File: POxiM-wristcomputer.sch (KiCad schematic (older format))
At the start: 25 parts, among them J1 USB_B_Micro, J10 Transmissivity in, J11 AudioJack4_Ground, J2 AudioJack4_Ground, J3 USB_B_Micro, J4 USB_A, J5 USB_A, J6 Uart Out, J7 Programming Header, J8 USB_B_Micro, J9 Interference in

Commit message: Start new LED drive method, some cleanup
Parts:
- removed J10: Transmissivity in, Connector_Coaxial:SMA_Molex_73251-2200_Horizontal, symbol Connector:Conn_Coaxial
- removed J11, J2: AudioJack4_Ground, POxiM-uncategorised:CUI_SJ-43514-SMT, symbol Connector:AudioJack4_Ground
- removed J3, J8: USB_B_Micro, POxiM-uncategorised:Micro-B_Molex_105017-0001, symbol Connector:USB_B_Micro
- removed J4, J5: USB_A, POxiM-uncategorised:USBA_87583-2010RLF, symbol Connector:USB_A
- removed J6: Uart Out, Connector_PinHeader_2.54mm:PinHeader_1x02_P2.54mm_Vertical, symbol Connector:Conn_01x02_Male
- removed J7: Programming Header, Connector_PinHeader_2.54mm:PinHeader_2x05_P2.54mm_Vertical, symbol Connector:Conn_01x10_Male
- removed J9: Interference in, Connector_Coaxial:SMA_Molex_73251-2200_Horizontal, symbol Connector:Conn_Coaxial
- removed MB1, MB2, MB3, MB4, MB5, MB6, MB7, MB8: Bumpon, POxiM-uncategorised:Bumpon-SJ-5007BK, symbol POxiM-mechanical:Bumpon
- added J?: To finger probe, POxiM-uncategorised:CUI_SJ-43514-SMT, symbol Connector:AudioJack4
- J1: value USB_B_Micro -> Power in
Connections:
- net labels removed: 5V_power_input
- wire segments 92 -> 32
- no-connect marks 11 -> 1
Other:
- note added: "Audio\npinout:"
- note added: "Ground"
- note added: "Left"
- note added: "Mechanical"
- note added: "Mic"
- note added: "Right"
- note removed: "Finger pretender board"
- note removed: "Programming board"
- note removed: "for audio:\nmic\ngnd\nright\nleft\n"
- moved on the sheet: H1, H2, H3, H4, H5, H6, J1

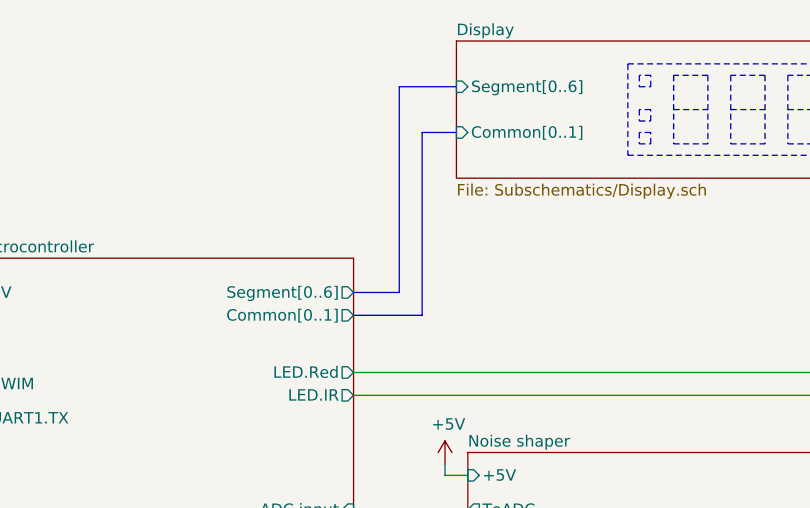
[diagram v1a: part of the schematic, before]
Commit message: Finish signal conditioning cleanup, start reworking display
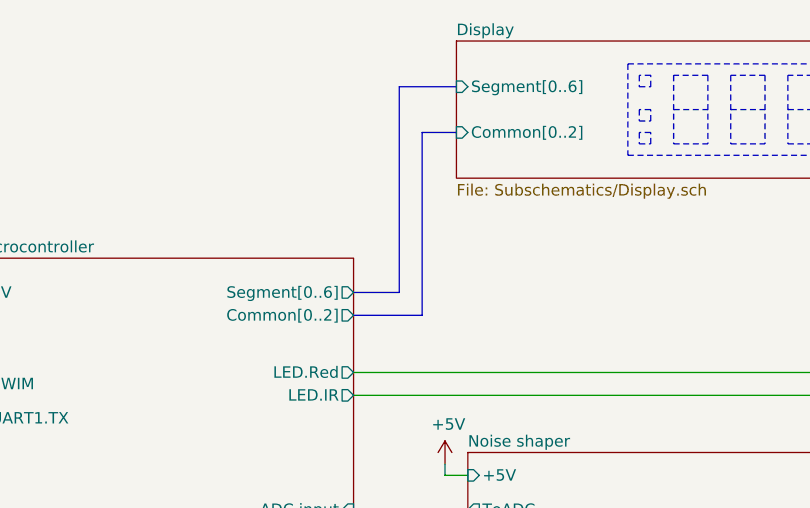
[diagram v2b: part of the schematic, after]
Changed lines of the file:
@@
 F1 "Subschematics/Display.sch" 50
 F2 "Segment[0..6]" I L 5750 2400 50
-F3 "Common[0..1]" I L 5750 2600 50
+F3 "Common[0..2]" I L 5750 2600 50
 $EndSheet
 $Sheet
@@
 F3 "5V" I L 3650 3300 50
 F4 "Segment[0..6]" O R 5300 3300 50
-F5 "Common[0..1]" O R 5300 3400 50
-F6 "ADC.feedback" O R 5300 4350 50
-F7 "ADC.input" I R 5300 4250 50
-F8 "LED.IR" O R 5300 3750 50
-F9 "LED.Red" O R 5300 3650 50
-F10 "UART1.TX" O L 3650 3850 50
-F11 "SWIM" B L 3650 3700 50
+F5 "ADC.feedback" O R 5300 4350 50
+F6 "ADC.input" I R 5300 4250 50
+F7 "LED.IR" O R 5300 3750 50
+F8 "LED.Red" O R 5300 3650 50
+F9 "UART1.TX" O L 3650 3850 50
+F10 "SWIM" B L 3650 3700 50
+F11 "Common[0..2]" O R 5300 3400 50
 $EndSheet
 Wire Wire Line

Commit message: Cleanup most of schematic
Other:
- note added: "Bibliography"
- note added: "How it works"
- note added: "In response to shortages during the Covid-19 pandemic, TU Delft is \ndeveloping the POxiM transmissive pulse oximeter. A pulse oximeter is a \nmedical instrument which doctors use to monitor the heart rate and blood \noxygen saturation of patients during critical stages of and revalidation from \nCovid-19. POxiM is intended to be fully qualified for use leading up to and \nafter intensive care, t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"
- note added: "Introduction"
- note added: "POxiM is based on the tranmissive pulse oximetry principle. This means that \nit determines the patient’s heart rate and blood oxygen concentration \n(SPO2) by measuring the portion of red (660nm) and infrared (940nm) light \nthat passes through their finger.\n\nThis is enabled by two effects. First, the optical properties of hemoglobin \nchange when it bonds with oxygen, so that blood with a hig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"
- note added: "Power budget"
- note added: "The physical system"
- note added: "There is 100mA available from a\nsingle power unit of USB. It is\nallocated as follows:\n - Microcontroller: 5mA\n - Readout circuit amplifier: 1mA\n - Readout LEDs: 2 · 10mA = 20mA\n - Display: 74mA\n - Digits: 7 · 10mA = 70mA\n - Transistor biasing: 4mA"
- note added: "There is only a single optical channel to avoid the cost of optical filters and \nmultiple channels. This introduces a problem, since the channel must be \nshared between the two wavelengths. Since the noise shaping circuitry is not \ncompatible with sharing the channel in time, the channel is shared in the \nfrequency domain. This is achieved by modulating each wavelength at a \nunique carrier f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"
- note added: "This design was informed by NXP’s AN4327 appnote, TI’s SLAA655, \nSLAA274, and SLAA458 appnotes, and TI’s TIDA-00311 reference design."
- note added: "ToDo:\n - Add top-level descriptions to each sheet.\n - Improve noise shaper description.\n - Update component values for Vin ∈ [4.5, 5.5]V\n - Check PWM output harmonics actually have 60dB down, and consider adding image\n - Explain microcontroller choice"
- moved on the sheet: J1, J?

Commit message: Start reworking sing supply ripple issues.
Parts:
- added FID? (x4): Fiducial, Fiducial:Fiducial_0.5mm_Mask1mm, symbol Mechanical:Fiducial
- H1, H2, H3, H4, H5, H6: Notes (none) -> SHOULD NOT BE ON BOM
- J1: Link (none) -> https://nl.mouser.com/ProductDetail/Molex/105017-0001?qs=%2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; Mfr. Molex -> (none); Mfr. No. 105017-0001 -> (none); Mouser No. 538-105017-0001 -> (none); Order number (none) -> 538-105017-0001; Part number (none) -> 105017-0001; Supplier (none) -> Mouser
- gave numbers to parts that had none: 1
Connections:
- net +5V: no longer J2.R2
- net GND: now also J2.R2
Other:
- note added: "# ToDo\n### Schematic\n - [x] Rework display LEDs to open drain\n - [x] Add LDO\n - [x] Feed noise shaper from LDO, so it cannot damage microcontroller\n - [x] Add DAC buffer\n - [ ] Add IR/red LED supply current isolation\n - [ ] Check if Zener voltage needs to change to incorporate lower supply voltage\n - [ ] Change noise shaper + in to ground\n - [ ] Update prediction inversion\n - [ ] Change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"
- note added: "Change stereo connector?\nIk zal even rondkijken voor 3,5m stereo jack connectoren. De CUI SJ-43514 \nis een connector die ik gisteren ook tegen kwam. Dit is zeker een optie."
- note added: "De USB-connectoren die wij hier momenteel op voorraad hebben liggen:\n - ZX62D-B-5PA8 Hirose\n - 10104110-0001LF FCI (Geheel SMD, dus het liefste vastklemmen)\n - 629105136821 WUERTH (Geheel SMD, dus het liefste vastklemmen)\n - 10118194-0001L FCI"
- note added: "Microcontroller needs 3.3V LDO, since required 40dB PSRR @ 5mA cannot \nbe easily achieved with capacitance multiplier at low frequencies and small \ncapacitors, whereas a voltage reference PSRR gets better at lower \nfrequencies.\n\nLED currents should be passed through ground so that only ground bond \nwire resistance is a factor, and the 1Ω output impedance of the LDO isn’t a \nproblem.\n\nLED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"
- note added: "To muntz:\n - Test whether LED driver RC delay is really necessary."
- moved on the sheet: H1, H2, H3, H4, H5, H6

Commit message: Initial PCB layout
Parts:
- FID1, FID2, FID3, FID4: renamed from FID?; Notes (none) -> SHOULD NOT BE ON BOM
- H1, H2, H3, H4: footprint MountingHole:MountingHole_2.2mm_M2_DIN965 -> POxiM-uncategorised:MountingHole_2.2mm_M2
- H5, H6: footprint MountingHole:MountingHole_2.2mm_M2_DIN965 -> POxiM-uncategorised:AlignmentHole_2.2mm_M2
- J1: footprint POxiM-uncategorised:Micro-B_Molex_105017-0001 -> POxiM-uncategorised:USB_Micro-B_Amphenol_10103594-0001LF_Horizontal; Link https://nl.mouser.com/ProductDetail/Molex/105017-0001?qs=%2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 -> https://nl.mouser.com/ProductDetail/Amphenol-FCI/10103594-0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; Order number 538-105017-0001 -> 649-10103594-0001LF; Part number 105017-0001 -> 10103594-0001LF
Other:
- note added: "# ToDo\n### Schematic\n - [x] Rework display LEDs to open drain\n - [x] Add LDO\n - [x] Feed noise shaper from LDO, so it cannot damage microcontroller\n - [x] Add DAC buffer\n - [x] Add IR/red LED supply current isolation\n - [x] Change noise shaper + in to ground\n - [x] Update prediction inversion\n - [x] Check if Zener voltage needs to change to incorporate lower supply voltage\n - [x] Change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"
- note added: "To muntz:\n - Test whether LED driver RC delay is really necessary.\n - LED display decoupling"
- note removed: "# ToDo\n### Schematic\n - [x] Rework display LEDs to open drain\n - [x] Add LDO\n - [x] Feed noise shaper from LDO, so it cannot damage microcontroller\n - [x] Add DAC buffer\n - [ ] Add IR/red LED supply current isolation\n - [ ] Check if Zener voltage needs to change to incorporate lower supply voltage\n - [ ] Change noise shaper + in to ground\n - [ ] Update prediction inversion\n - [ ] Change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"
- note removed: "Microcontroller needs 3.3V LDO, since required 40dB PSRR @ 5mA cannot \nbe easily achieved with capacitance multiplier at low frequencies and small \ncapacitors, whereas a voltage reference PSRR gets better at lower \nfrequencies.\n\nLED currents should be passed through ground so that only ground bond \nwire resistance is a factor, and the 1Ω output impedance of the LDO isn’t a \nproblem.\n\nLED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"
- note removed: "To muntz:\n - Test whether LED driver RC delay is really necessary."
- note removed: "ToDo:\n - Add top-level descriptions to each sheet.\n - Improve noise shaper description.\n - Update component values for Vin ∈ [4.5, 5.5]V\n - Check PWM output harmonics actually have 60dB down, and consider adding image\n - Explain microcontroller choice"

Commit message: Finalise wrist computer rev A
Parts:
- added NT1, NT2: Net-Tie_2, NetTie:NetTie-2_SMD_Pad0.5mm, symbol Device:Net-Tie_2
- FID1, FID2, FID3, FID4: footprint Fiducial:Fiducial_0.5mm_Mask1mm -> POxiM-uncategorised:Fiducial_1mm_Mask2mm
- H1, H2, H3, H4: footprint POxiM-uncategorised:MountingHole_2.2mm_M2 -> MountingHole:MountingHole_2.2mm_M2
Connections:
- net GND: now also NT1.1, NT2.1; no longer J2.R2
- new net GNDA: J2.R2, NT2.2
- new net GNDREF: NT1.2
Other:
- moved on the sheet: J2

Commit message: Update BOM
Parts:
- NT1, NT2: Notes (none) -> SHOULD NOT BE ON BOM
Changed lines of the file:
@@
 F 2 "NetTie:NetTie-2_SMD_Pad0.5mm" H 5550 6150 50  0001 C CNN
 F 3 "~" H 5550 6150 50  0001 C CNN
+F 4 "SHOULD NOT BE ON BOM" H 0   0   50  0001 C CNN "Notes"
 	1    5550 6150
 	1    0    0    -1
@@
 F 2 "NetTie:NetTie-2_SMD_Pad0.5mm" H 7550 6150 50  0001 C CNN
 F 3 "~" H 7550 6150 50  0001 C CNN
+F 4 "SHOULD NOT BE ON BOM" H 0   0   50  0001 C CNN "Notes"
 	1    7550 6150
 	1    0    0    -1

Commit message: Finish first schematic version
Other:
- note added: "### Documentation\n - [ ] Consider re-ordering sheets\n - [ ] Remove superfluous datasheets\n - [ ] Explain why 80Hz PWM has proper components.\n - [ ] Better spacing of main sheet\n - [ ] Re-evaluate capacitor voltages, since they’re used in protection chain.\n - [ ] Add CLKOUT testpoint for clock trimming\n - [ ] Consider addings testpoints for ADC feedback units\n - [ ] Add top-level descripti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"
- note added: "### Documentation\n - [x] Explain microcontroller choice\n - [x] Fix remapped microcontroller pins\n - [x] Update open drain segment warning in LED sheet for changed segment numbering\n - [x] Update LED driver description of filter to use LED resistance.\n - [x] Update photodiode input protection.\n - [x] Update programming interface\n - [x] Flip constant current LED transistors\n - [x] LDO enabl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"
- note added: "Changelog"
- note added: "Production"
- note added: "Rev A.0: Completed first iteration\nRev A.1: Incorporated small learnings from first full prototype"
- note added: "There is only a single optical channel to avoid the cost of optical filters and \nmultiple channels. This introduces a problem, since the channel must be \nshared between the two wavelengths. Since the noise shaping circuitry is not \ncompatible with sharing the channel in time, the channel is shared in the \nfrequency domain. This is achieved by Quadrature Amplitude Modulation \n(QAM): the wavel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"
- note added: "To muntz:\n - Test whether LED driver RC delay is really necessary.\n - LED display decoupling\n - LED driver 33kΩ bias resistor required, since LED discharge speed is limited?"
- note removed: "De USB-connectoren die wij hier momenteel op voorraad hebben liggen:\n - ZX62D-B-5PA8 Hirose\n - 10104110-0001LF FCI (Geheel SMD, dus het liefste vastklemmen)\n - 629105136821 WUERTH (Geheel SMD, dus het liefste vastklemmen)\n - 10118194-0001L FCI"
- note removed: "There is only a single optical channel to avoid the cost of optical filters and \nmultiple channels. This introduces a problem, since the channel must be \nshared between the two wavelengths. Since the noise shaping circuitry is not \ncompatible with sharing the channel in time, the channel is shared in the \nfrequency domain. This is achieved by modulating each wavelength at a \nunique carrier f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"
- note removed: "To muntz:\n - Test whether LED driver RC delay is really necessary.\n - LED display decoupling"
- moved on the sheet: FID1, FID2, FID3, FID4, H1, H2, H3, H4, H5, H6
